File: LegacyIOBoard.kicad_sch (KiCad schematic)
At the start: 71 parts, among them J1 350826-1, J10 AFBR-59R5LZ, J11 AFBR-59R5LZ, J12 AFBR-59R5LZ, J13 AFBR-59R5LZ, J2 A_In, J3 A_Out, J4 D_In, J5 D_Out, J6 B_In, J7 B_Out, J8 C_In, J9 C_Out, K1 1-1393210-3, K11 G5LE-1-VD-DC12, K2 1-1393210-3, K3 1-1393210-3, K4 1-1393210-3, K5 HE722A1200, K6 HE722A1200, K7 HE722A1200, K8 HE722A1200, K9 G5LE-1-VD-DC12, U1 AP64501SP-13, U10 DMN3023L-7, U11 DMN3023L-7, U2 AP3211KTR-G1, U3 SC0192_9_, U4 DMN3023L-7, U5 DMN3023L-7, U6 DMN3023L-7, U7 DMN3023L-7, U8 DMN3023L-7, U9 SFH615A-4X009

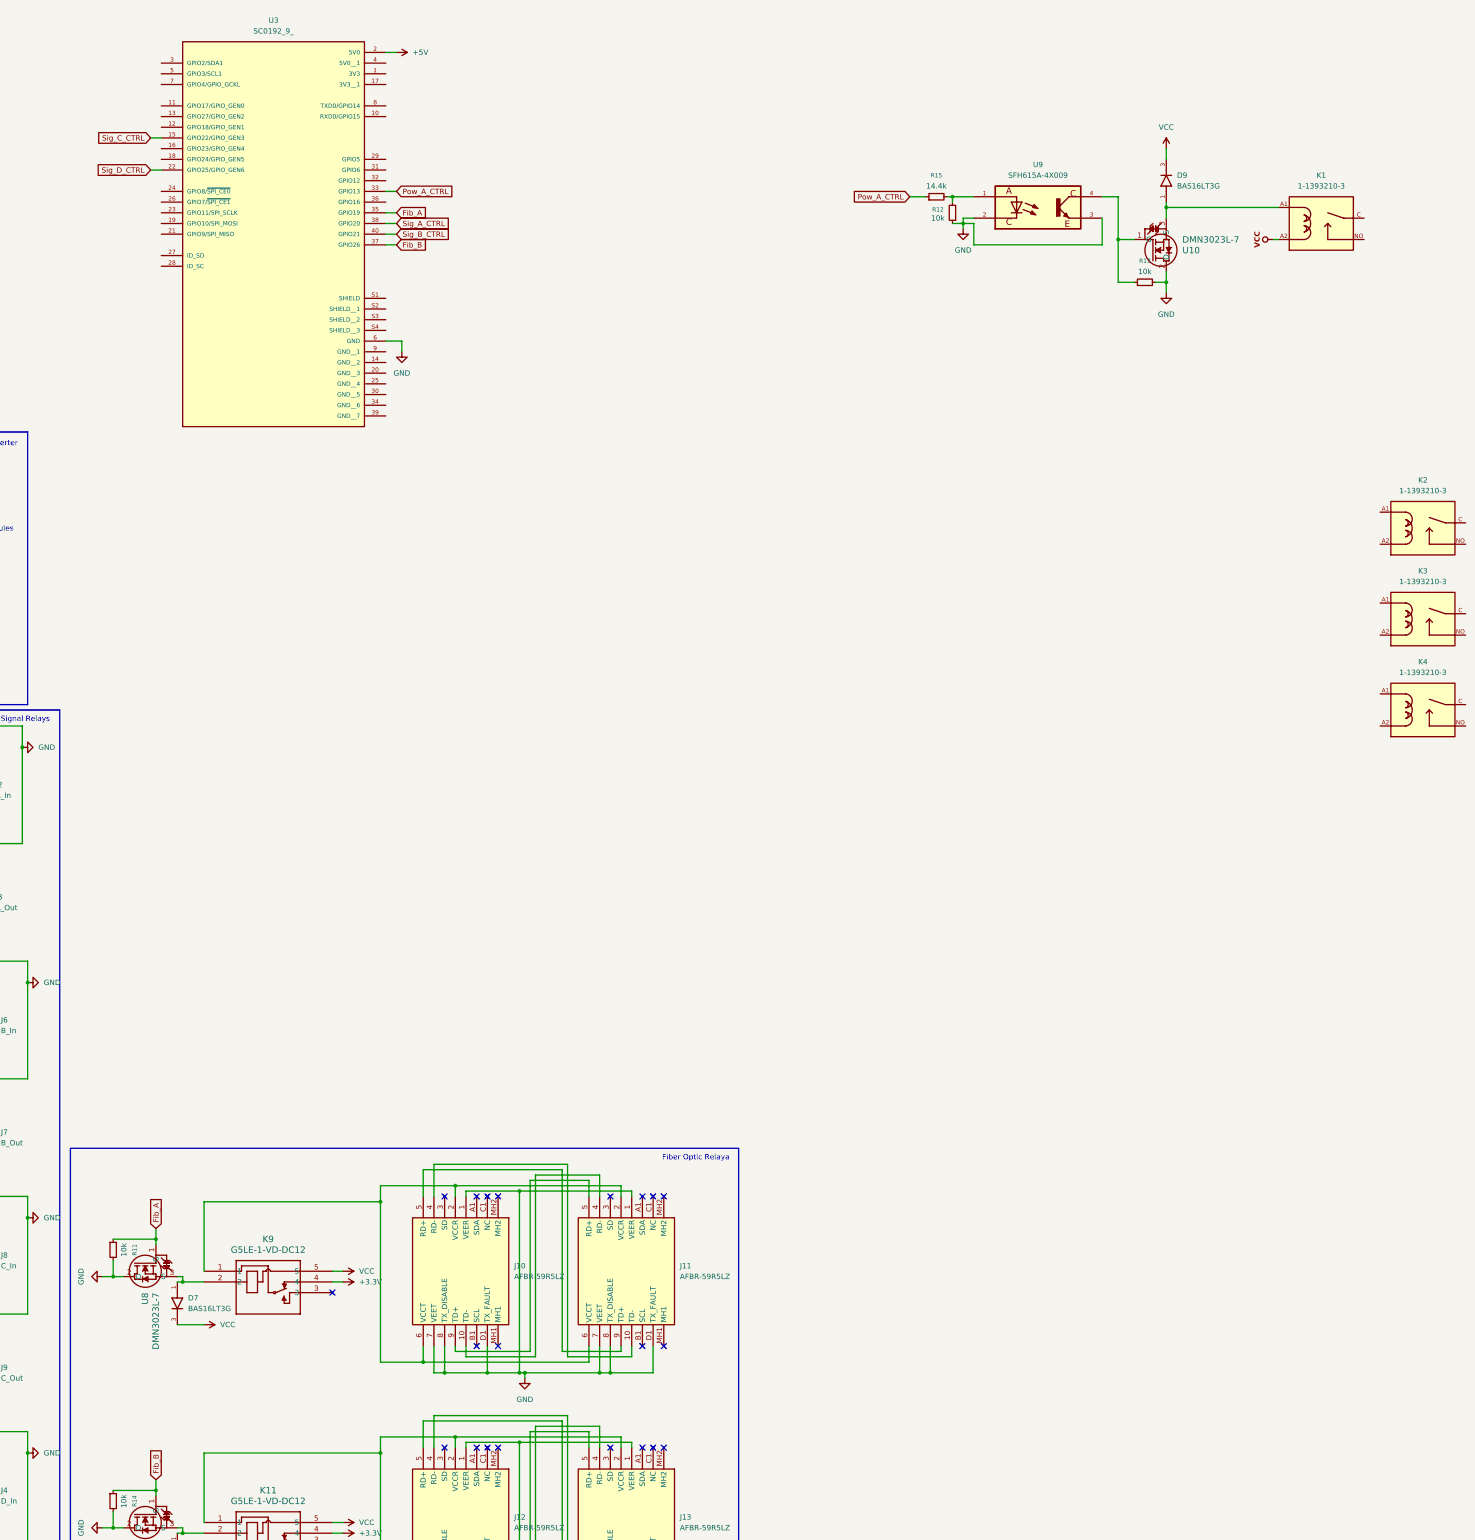
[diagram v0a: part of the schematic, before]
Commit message: Ref #1 Added more power relays and organized them.
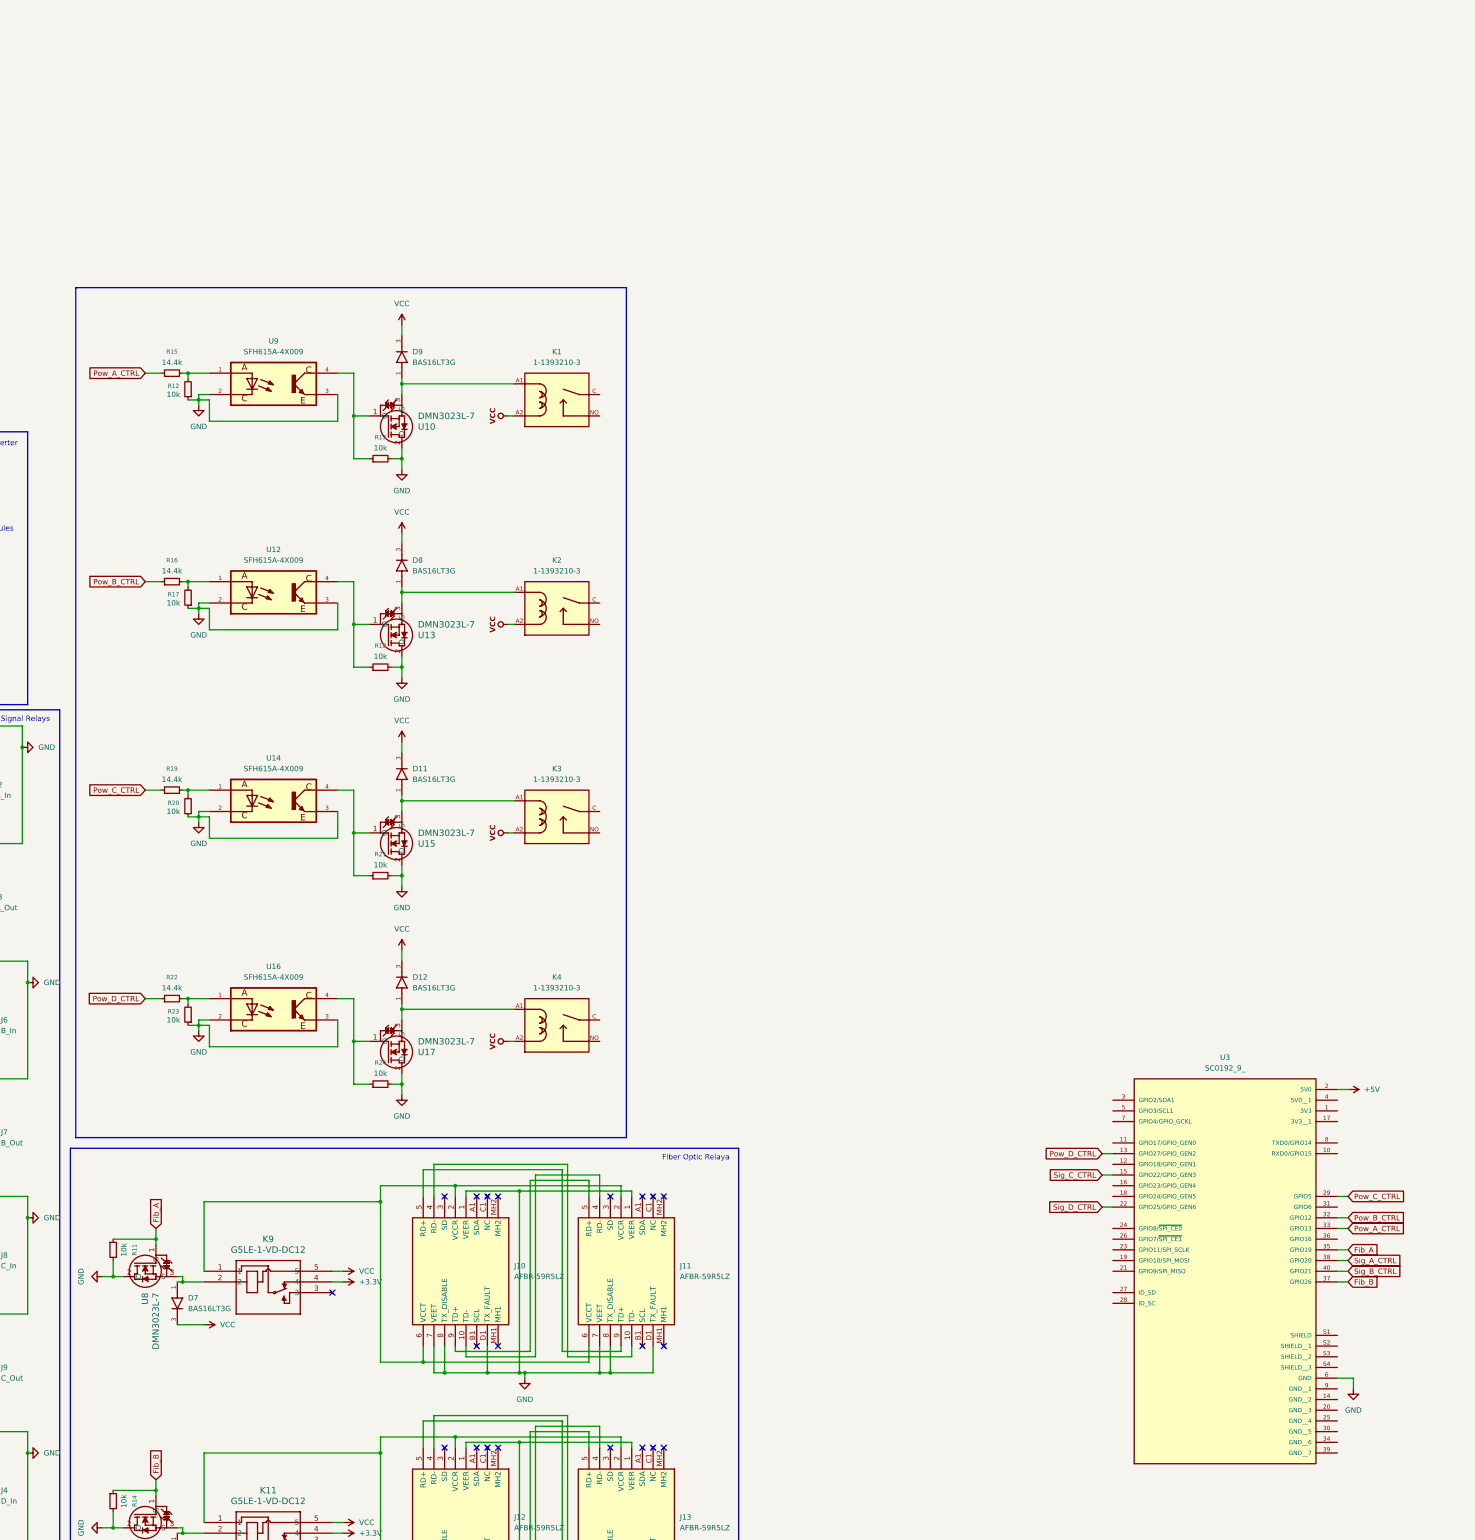
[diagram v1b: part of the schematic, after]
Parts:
- added D11, D12, D8: BAS16LT3G, BAS16LT3G:SOT95P240X111-3N, symbol BAS16LT3G:BAS16LT3G
- added R16, R19, R22: 14.4k, symbol Device:R_Small
- added R17, R18, R20, R21, R23, R24: 10k, symbol Device:R_Small
- added U12, U14, U16: SFH615A-4X009, SFH615A-4X009:SOIC254P1016X390-4N, symbol SFH615A-4X009:SFH615A-4X009
- added U13, U15, U17: DMN3023L-7, SOT-23_2P9X1P3_DIO, symbol 2025-06-16_16-08-42:DMN3023L-7
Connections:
- net GND: now also R17.1, R18.2, R20.1, R21.2, R23.1, R24.2, U12.2, U12.3, U13.2 (D), U14.2, U14.3, U15.2 (D), U16.2, U16.3, U17.2 (D)
- net VCC: now also K2.A2, K3.A2, K4.A2, D11.3, D12.3, D8.3
- net at K4.A1: now also D12.1, U17.3 (S)
- net Pow_D_CTRL: now reaches U3.13 (GPIO27/GPIO_GEN2)
- net Pow_D_CTRL: now also R22.1
- net Pow_C_CTRL: now reaches U3.29 (GPIO5)
- net Pow_C_CTRL: now also R19.1
- net Pow_B_CTRL: now reaches U3.32 (GPIO12)
- net Pow_B_CTRL: now also R16.1
- net at K2.A1: now also D8.1, U13.3 (S)
- net at K3.A1: now also D11.1, U15.3 (S)
- new net: R18.1, U12.4, U13.1 (G)
- new net: R22.2, R23.2, U16.1
- new net: R19.2, R20.2, U14.1
- new net: R21.1, U14.4, U15.1 (G)
- new net: R24.1, U16.4, U17.1 (G)
- new net: R16.2, R17.2, U12.1
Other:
- moved on the sheet: D9, K1, R12, R13, R15, U10, U3, U9

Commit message: Ref 2 Added 3 pin connectors. Added LEDs for outputs. Organized schematic.
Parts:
- added D13, D17, D18, D19, D20, D21, D22, D23, D24, D25: LED, symbol opto:LED
- added J14, J15, J16, J17, J18, J19, J20, J21: 10845031, CONN_SDA_42002-xxxxx_03_MOL, symbol 2025-06-19_16-23-33:10845031
- added R25, R29, R30, R31, R32, R33, R34, R35, R36, R37: 1k, symbol Device:R_Small
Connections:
- net GND: now also D13.K, D17.K, D18.K, D19.K, D20.K, D21.K, D22.K, D23.K, D24.K, D25.K, J14.1, J15.1, J16.1, J17.1, J18.1, J19.1, J20.1, J21.1
- net at D4.1, K6.6, U5.3 (S): now also R30.1
- net at D5.1, K7.6, U6.3 (S): now also R31.1
- net at J10.2 (VCCR), J10.6 (VCCT), J11.2 (VCCR)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: now also R33.1
- net at D9.1, K1.A1, U10.3 (S): now also R35.2
- net at K1.C: now also J14.2
- net at K1.NO: now also J18.2
- net at D11.1, K3.A1, U15.3 (S): now also R36.2
- net at D12.1, K4.A1, U17.3 (S): now also R37.2
- net at K4.C: now also J20.2
- net at K4.NO: now also J21.2
- net at D6.1, K8.6, U7.3 (S): now also R32.1
- net at D8.1, K2.A1, U13.3 (S): now also R25.2
- net at J12.2 (VCCR), J12.6 (VCCT), J13.2 (VCCR)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: now also R34.1
- net at K2.C: now also J15.2
- net at K2.NO: now also J16.2
- net at D3.1, K5.6, U4.3 (S): now also R29.1
- net at K3.C: now also J17.2
- net at K3.NO: now also J19.2
- new net: D25.A, R37.1
- new net: J20.3, J21.3
- new net: D13.A, R25.1
- new net: D21.A, R33.2
- new net: J17.3, J19.3
- new net: D17.A, R29.2
- new net: D19.A, R31.2
- new net: D23.A, R35.1
- new net: J15.3, J16.3
- new net: D18.A, R30.2
- new net: D22.A, R34.2
- new net: J14.3, J18.3
- new net: D20.A, R32.2
- new net: D24.A, R36.1
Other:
- note added: "AC Input (to Wall)"
- note added: "AC Output"
- note added: "AC Power Relays"
- note added: "FO out"
- note added: "Optocoupler"
- note added: "PL out"
- note added: "Raspberry Pi 4"
- note added: "Vin"
- note added: "Vout"
- moved on the sheet: C1, C10, C2, C3, C4, C4_(Optional), C5, C6, C7, C8, C9, D1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

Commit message: Ref 3 Replaced AC power relays with ones that have normally closed terminals. Added SATA jacks, and mod debug port.
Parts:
- removed D18, D19, D20: LED, symbol opto:LED
- removed D5: BAS16LT3G, BAS16LT3G:SOT95P240X111-3N, symbol BAS16LT3G:BAS16LT3G
- removed J4: D_In, symbol Connector:RJ45_Shielded
- removed J5: D_Out, symbol Connector:RJ45_Shielded
- removed J8: C_In, symbol Connector:RJ45_Shielded
- removed J9: C_Out, symbol Connector:RJ45_Shielded
- removed K1, K2, K3, K4: 1-1393210-3, 1-1393210-3:TE_1-1393210-3, symbol 1-1393210-3:1-1393210-3
- removed K8: HE722A1200, HE722_LTF, symbol 2025-06-16_15-48-50:HE722A1200
- added D14, D16, D5: LED, symbol opto:LED
- added D15: BAS16LT3G, BAS16LT3G:SOT95P240X111-3N, symbol BAS16LT3G:BAS16LT3G
- added J22, J23, J26, J27, J30, J4, J5, J8, J9: 678005005, CONN_67800-5005_MOL, symbol 2025-06-19_19-31-31:678005005
- added J24, J28: A_In, symbol Connector:RJ45_Shielded
- added J25, J29: A_Out, symbol Connector:RJ45_Shielded
- added K1, K10, K2, K3: PR23-12V-900-1C, PR23-12V-900-1C:RELAY_PR23-12V-900-1C, symbol PR23-12V-900-1C:PR23-12V-900-1C
- added K4: HE722A1200, HE722_LTF, symbol 2025-06-16_15-48-50:HE722A1200
- added R26, R27, R28, R38, R39, R40, R41, R42, R43, R44, R45, R46, R49, R50, R51, R52, R53, R54, R55, R56, R59, R60, R61, R62, R63, R64, R65, R66: 0, symbol Device:R_Small
- added R47, R57: 10k, symbol Device:R_Small
- added R48, R58: 1k, symbol Device:R_Small
- J6: value B_In -> A_In
- J7: value B_Out -> A_Out
- R10: value 10k -> 0
- R30, R31, R32: value 1k -> 0
- R9: value 10k -> 1k
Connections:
- net GND: now also D14.K, D16.K, D5.K, J24.SH, J25.SH, J28.SH, J29.SH, K1.NO, K10.NO, K2.NO, K3.NO, R47.2, R57.2; no longer R10.2, R9.2
- net Sig_C_CTRL: now also R47.1; no longer R9.1
- net Sig_D_CTRL: now also R57.1; no longer R10.1
- net VCC: now also D15.3, K1.A2, K10.A2, K2.A2, K3.A2, K4.2
- net at D12.1, R37.2, U17.3 (S): now also K3.A1
- net at J6.1, J7.3: now also R45.2; no longer K6.8
- net at J6.2, J7.6: now also R44.2; no longer K6.14
- net at J6.3, J7.1: now also R46.2; no longer K6.7
- net at J6.6, J7.2: now also R43.2; no longer K6.1
- net at J20.2: now also K3.NC
- net at J21.2: now also K3.COM_1, K3.COM_2
- net at D8.1, R25.2, U13.3 (S): now also K1.A1
- net at J19.2: now also K2.COM_1, K2.COM_2
- net at R31.2: now also J4.3, J5.5
- net at D4.1, U5.3 (S): now also R9.1, K4.6; no longer K6.6, R30.1
- net at D9.1, R35.2, U10.3 (S): now also K10.A1
- net at J16.2: now also K1.COM_1, K1.COM_2
- net at R30.2: now also J4.5, J5.3
- net at J14.2: now also K10.NC
- net at J18.2: now also K10.COM_1, K10.COM_2
- net at D11.1, R36.2, U15.3 (S): now also K2.A1
- net at J2.1, J3.3: now also R40.2; no longer K5.8
- net at J2.2, J3.6: now also R41.2; no longer K5.14
- net at J2.3, J3.1: now also R39.2; no longer K5.7
- net at J2.6, J3.2: now also R42.2; no longer K5.1
- net at K7.1: now also R62.1, R63.1
- net at K7.14: now also R60.1, R64.1
- net at K7.7: now also R61.1, R66.1
- net at K7.8: now also R59.1, R65.1
- net at R32.2: now also J4.2, J5.6
- net at J15.2: now also K1.NC
- net at J17.2: now also K2.NC
- new net: D6.1, K6.6, R48.1, U6.3 (S)
- new net: J26.2, J27.6, R62.2
- new net: K6.14, R50.1, R54.1
- new net: J8.5, J9.3, R50.2
- new net: K5.14, R27.1, R41.1
- new net: J22.5, J23.3, R27.2
- new net: D5.A, R9.2
- new net: K4.14, R30.1, R44.1
- new net: J26.5, J27.3, R60.2
- new net: D15.1, K7.6, R58.1, U7.3 (S)
- new net: J26.1, J27.7
- new net: J26.3, J27.5, R61.2
- new net: J26.4, J27.4
- new net: J26.6, J27.2, R59.2
- new net: J26.7, J27.1
- new net: D16.A, R58.2
- new net: K6.8, R49.1, R55.1
- new net: J24.1, J25.3, R55.2
- new net: J4.7, J5.1
- new net: J4.6, J5.2, R10.2
- new net: J4.4, J5.4
- new net: J4.1, J5.7
- new net: K5.1, R38.1, R42.1
- new net: K5.7, R28.1, R39.1
- new net: J28.1, J29.3, R65.2
- new net: J28.2, J29.6, R64.2
- new net: J28.3, J29.1, R66.2
- new net: J28.4, J29.7
- new net: J28.5, J29.8
- new net: J28.6, J29.2, R63.2
- new net: J28.7, J29.4
- new net: J28.8, J29.5
- new net: J22.3, J23.5, R28.2
- new net: K5.8, R26.1, R40.1
- new net: K6.1, R52.1, R53.1
- new net: K6.7, R51.1, R56.1
- new net: K4.1, R32.1, R43.1
- new net: K4.8, R10.1, R45.1
- new net: J8.3, J9.5, R51.2
- new net: K4.7, R31.1, R46.1
- new net: J22.6, J23.2, R26.2
- new net: J24.2, J25.6, R54.2
- new net: D14.A, R48.2
- new net: J8.6, J9.2, R49.2
- new net: J22.7, J23.1
- new net: J22.4, J23.4
- new net: J22.2, J23.6, R38.2
- new net: J22.1, J23.7
- new net: J24.3, J25.1, R56.2
- new net: J24.6, J25.2, R53.2
- new net: J24.7, J25.4
- new net: J24.8, J25.5
- new net: J24.4, J25.7
- new net: J24.5, J25.8
- new net: J8.7, J9.1
- new net: J8.4, J9.4
- new net: J8.2, J9.6, R52.2
- new net: J8.1, J9.7
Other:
- moved on the sheet: C1, C10, C2, C3, C4, C4_(Optional), C5, C6, C7, C8, C9, D1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

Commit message: Ref 4 Corrected optocoupler circuits for proper MOSFET control. Wired debug jack. Replaced origional 5V buck converter with the 3.3V buck converter and modified it to output 5V (both buck converters are the same chip, just different outputs).
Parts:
- removed J30: 678005005, CONN_67800-5005_MOL, symbol 2025-06-19_19-31-31:678005005
- removed R20, R23: 10k, symbol Device:R_Small
- added C11: 10nF, symbol Device:C_Small
- added C12: 10uF, symbol Device:C_Small
- added C13: 22uF, symbol Device:C_Small
- added D18: 1N4148WT, Diode_SMD:D_SOD-523, symbol Diode:1N4148WT
- added J31: B08B-PASKLFSN, CONN_B08B-PASK_JST, symbol 2025-06-19_20-51-02:B08B-PASKLFSN
- added L3: 4.7uH, symbol Device:L_Small
- added U18: AP3211KTR-G1, SOT23-6_DIO, symbol 2025-06-13_17-05-22:AP3211KTR-G1
- R12: value 10k -> 49.9k
- R15, R16, R19, R22: value 14.4k -> 244
- R17: value 10k -> 16.3k
- R5: value 49.9k -> 51.7k
- R6: value 16.3k -> 10k
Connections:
- net +3.3V: now also R12.2, C13.1, L3.2; no longer C10.1, L2.2, R5.2
- net +5V: now also U12.4, U14.4, U16.4, U9.4
- net GND: now also C12.2, C13.2, D18.2 (A), J31.2, U18.2 (GND); no longer R12.1, U12.3, U14.3, U16.3, U9.3
- net VCC: now also C12.1, U18.4 (EN), U18.5 (IN)
- net Target_RX: now reaches U3.10 (RXD0/GPIO15)
- net Target_RX: now also J31.6
- net Target_TX: now reaches U3.8 (TXD0/GPIO14)
- net Target_TX: now also J31.5
- net at R18.1, U13.1 (G): now also U12.3; no longer U12.4
- net at R21.1, U15.1 (G): now also U14.3; no longer U14.4
- net at R24.1, U17.1 (G): now also U16.3; no longer U16.4
- net at R15.2, U9.1: no longer R12.2
- net at R16.2, U12.1: no longer R17.2
- net at R13.1, U10.1 (G): now also U9.3; no longer U9.4
- new net: R12.1, R17.2, U18.3 (FB)
- new net: C11.1, U18.1 (BS)
- new net: C11.2, D18.1 (K), L3.1, U18.6 (SW)
- new net 5V: C10.1, L2.2, R5.2
- no-connect marks 36 -> 41
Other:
- note added: "Mod Debug"
- note added: "RJ45 & SATA Signal Relays"
- note removed: "RJ45 Signal Relays"
- moved on the sheet: C1, C2, C3, C4, C4_(Optional), C5, C6, C7, D1, J1, L1, R1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

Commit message: Ref 5 Changed 12V to 5V buck converter to IC that outputs 3A. Added CSV file for BOM template.
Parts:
- removed C10, C6, C7: 22uF, symbol Device:C_Small
- removed C4_(Optional): 33pF, symbol Device:C_Small
- removed C8: 10uF, symbol Device:C_Small
- removed C9: 10nF, symbol Device:C_Small
- removed D2: 1N4148WT, Diode_SMD:D_SOD-523, symbol Diode:1N4148WT
- removed L2: 4.7uH, symbol Device:L_Small
- removed R5: 51.7k, symbol Device:R_Small
- removed R6: 10k, symbol Device:R_Small
- removed U1: AP64501SP-13, AP64501SP-13:SOIC127P600X170-9N, symbol AP64501SP-13:AP64501SP-13
- removed U2: AP3211KTR-G1, SOT23-6_DIO, symbol 2025-06-13_17-05-22:AP3211KTR-G1
- added R20: 1k, symbol Device:R_Small
- added U1: AP62300TWU-7, TSOT26-WU_DIO, symbol 2025-06-23_15-31-30:AP62300TWU-7
- C2: value 10nF -> 100nF
- C3: value 2.7nF -> 100pF
- C4: value 100nF -> 22uF
- L1: value 3.6uH -> 3.3uF
- R2: value 15.8k -> 56.2k
- R3: value 155k -> 10k
- R4: value 22.1k -> 9k
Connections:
- net +5V: no longer C5.1, L1.2, R3.2
- net 5V: now also C3.1, C4.1, C5.1, L1.2, R2.1
- net GND: now also C4.2, R3.2, R20.2, U1.1 (GND); no longer C2.2, C3.2, K1.NO, K10.NO, K2.NO, K3.NO, R4.1
- net VCC: now also R4.1, U1.3 (VIN)
- net at C2.1: now also L1.1, U1.2 (SW)
- net at R3.1: now also C3.2, R2.2, U1.4 (FB); no longer R4.2
- new net: R20.1, R4.2, U1.5 (EN)
- new net: C2.2, U1.6 (BST)
- no-connect marks 41 -> 45
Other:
- note added: "1.2V for Enable"
- note added: "Fiber Optic Relays"
- note added: "Vout to Pi"
- note removed: "Fiber Optic Relaya"
- note removed: "To Pi"
- moved on the sheet: C11, C12, C13, D1, D10, D11, D12, D13, D18, D21, D22, D23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
